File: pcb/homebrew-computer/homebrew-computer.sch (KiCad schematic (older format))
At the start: 0 parts

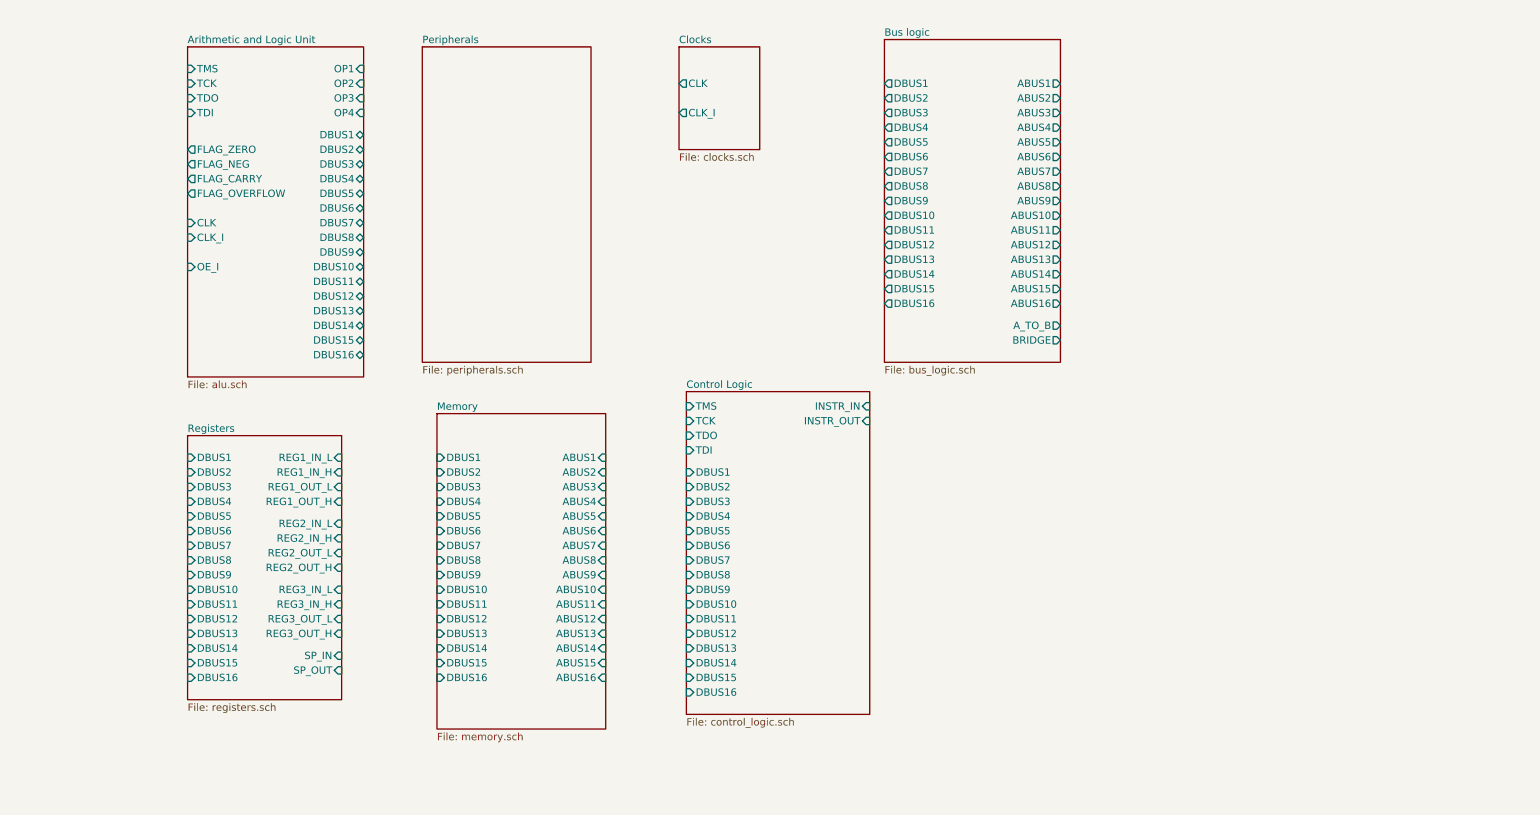
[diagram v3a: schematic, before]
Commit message: Add the memory interface logic
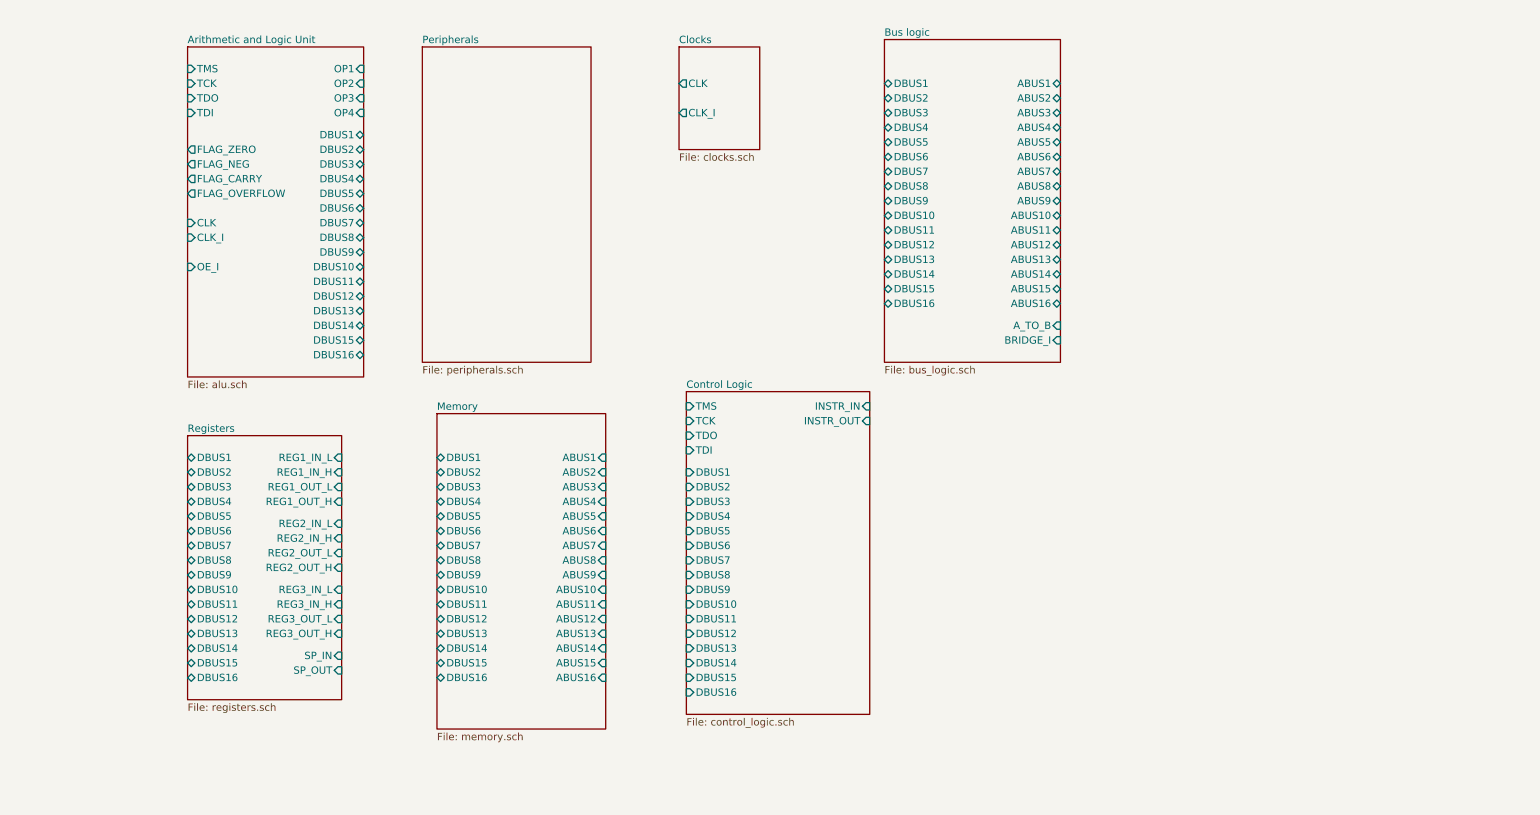
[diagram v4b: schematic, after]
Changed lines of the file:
@@
 F0 "Registers" 50
 F1 "registers.sch" 50
-F2 "DBUS1" I L 2250 3800 50
-F3 "DBUS2" I L 2250 3900 50
-F4 "DBUS3" I L 2250 4000 50
-F5 "DBUS4" I L 2250 4100 50
-F6 "DBUS5" I L 2250 4200 50
-F7 "DBUS6" I L 2250 4300 50
-F8 "DBUS7" I L 2250 4400 50
-F9 "DBUS8" I L 2250 4500 50
-F10 "DBUS9" I L 2250 4600 50
-F11 "DBUS10" I L 2250 4700 50
-F12 "DBUS11" I L 2250 4800 50
-F13 "DBUS12" I L 2250 4900 50
-F14 "DBUS13" I L 2250 5000 50
-F15 "DBUS14" I L 2250 5100 50
-F16 "DBUS15" I L 2250 5200 50
-F17 "DBUS16" I L 2250 5300 50
+F2 "DBUS1" B L 2250 3800 50
+F3 "DBUS2" B L 2250 3900 50
+F4 "DBUS3" B L 2250 4000 50
+F5 "DBUS4" B L 2250 4100 50
+F6 "DBUS5" B L 2250 4200 50
+F7 "DBUS6" B L 2250 4300 50
+F8 "DBUS7" B L 2250 4400 50
+F9 "DBUS8" B L 2250 4500 50
+F10 "DBUS9" B L 2250 4600 50
+F11 "DBUS10" B L 2250 4700 50
+F12 "DBUS11" B L 2250 4800 50
+F13 "DBUS12" B L 2250 4900 50
+F14 "DBUS13" B L 2250 5000 50
+F15 "DBUS14" B L 2250 5100 50
+F16 "DBUS15" B L 2250 5200 50
+F17 "DBUS16" B L 2250 5300 50
 F18 "REG1_IN_L" I R 3300 3800 50
 F19 "REG1_IN_H" I R 3300 3900 50
@@
 $EndSheet
 $Sheet
+S 5600 1000 550  700
+U 5F97DC64
+F0 "Clocks" 50
+F1 "clocks.sch" 50
+F2 "CLK" O L 5600 1250 50
+F3 "CLK_I" O L 5600 1450 50
+$EndSheet
+$Sheet
+S 7000 950  1200 2200
+U 5F97DCB2
+F0 "Bus logic" 50
+F1 "bus_logic.sch" 50
+F2 "DBUS1" B L 7000 1250 50
+F3 "DBUS2" B L 7000 1350 50
+F4 "DBUS3" B L 7000 1450 50
+F5 "DBUS4" B L 7000 1550 50
+F6 "DBUS5" B L 7000 1650 50
+F7 "DBUS6" B L 7000 1750 50
+F8 "DBUS7" B L 7000 1850 50
+F9 "DBUS8" B L 7000 1950 50
+F10 "DBUS9" B L 7000 2050 50
+F11 "DBUS10" B L 7000 2150 50
+F12 "DBUS11" B L 7000 2250 50
+F13 "DBUS12" B L 7000 2350 50
+F14 "DBUS13" B L 7000 2450 50
+F15 "DBUS14" B L 7000 2550 50
+F16 "DBUS15" B L 7000 2650 50
+F17 "DBUS16" B L 7000 2750 50
+F18 "ABUS1" B R 8200 1250 50
+F19 "ABUS2" B R 8200 1350 50
+F20 "ABUS3" B R 8200 1450 50
+F21 "ABUS4" B R 8200 1550 50
+F22 "ABUS5" B R 8200 1650 50
+F23 "ABUS6" B R 8200 1750 50
+F24 "ABUS7" B R 8200 1850 50
+F25 "ABUS8" B R 8200 1950 50
+F26 "ABUS9" B R 8200 2050 50
+F27 "ABUS10" B R 8200 2150 50
+F28 "ABUS11" B R 8200 2250 50
+F29 "ABUS12" B R 8200 2350 50
+F30 "ABUS13" B R 8200 2450 50
+F31 "ABUS14" B R 8200 2550 50
+F32 "ABUS15" B R 8200 2650 50
+F33 "ABUS16" B R 8200 2750 50
+F34 "A_TO_B" I R 8200 2900 50
+F35 "BRIDGE_I" I R 8200 3000 50
+$EndSheet
+$Sheet
 S 3950 3500 1150 2150
 U 5F95DC76
 F0 "Memory" 50
 F1 "memory.sch" 50
-F2 "DBUS1" I L 3950 3800 50
-F3 "DBUS2" I L 3950 3900 50
-F4 "DBUS3" I L 3950 4000 50
-F5 "DBUS4" I L 3950 4100 50
-F6 "DBUS5" I L 3950 4200 50
-F7 "DBUS6" I L 3950 4300 50
-F8 "DBUS7" I L 3950 4400 50
-F9 "DBUS8" I L 3950 4500 50
-F10 "DBUS9" I L 3950 4600 50
-F11 "DBUS10" I L 3950 4700 50
-F12 "DBUS11" I L 3950 4800 50
-F13 "DBUS12" I L 3950 4900 50
-F14 "DBUS13" I L 3950 5000 50
-F15 "DBUS14" I L 3950 5100 50
-F16 "DBUS15" I L 3950 5200 50
-F17 "DBUS16" I L 3950 5300 50
+F2 "DBUS1" B L 3950 3800 50
+F3 "DBUS2" B L 3950 3900 50
+F4 "DBUS3" B L 3950 4000 50
+F5 "DBUS4" B L 3950 4100 50
+F6 "DBUS5" B L 3950 4200 50
+F7 "DBUS6" B L 3950 4300 50
+F8 "DBUS7" B L 3950 4400 50
+F9 "DBUS8" B L 3950 4500 50
+F10 "DBUS9" B L 3950 4600 50
+F11 "DBUS10" B L 3950 4700 50
+F12 "DBUS11" B L 3950 4800 50
+F13 "DBUS12" B L 3950 4900 50
+F14 "DBUS13" B L 3950 5000 50
+F15 "DBUS14" B L 3950 5100 50
+F16 "DBUS15" B L 3950 5200 50
+F17 "DBUS16" B L 3950 5300 50
 F18 "ABUS1" I R 5100 3800 50
 F19 "ABUS2" I R 5100 3900 50
@@
 F33 "ABUS16" I R 5100 5300 50
 $EndSheet
-$Sheet
-S 5600 1000 550  700
-U 5F97DC64
-F0 "Clocks" 50
-F1 "clocks.sch" 50
-F2 "CLK" O L 5600 1250 50
-F3 "CLK_I" O L 5600 1450 50
-$EndSheet
-$Sheet
-S 7000 950  1200 2200
-U 5F97DCB2
-F0 "Bus logic" 50
-F1 "bus_logic.sch" 50
-F2 "DBUS1" O L 7000 1250 50
-F3 "DBUS2" O L 7000 1350 50
-F4 "DBUS3" O L 7000 1450 50
-F5 "DBUS4" O L 7000 1550 50
-F6 "DBUS5" O L 7000 1650 50
-F7 "DBUS6" O L 7000 1750 50
-F8 "DBUS7" O L 7000 1850 50
-F9 "DBUS8" O L 7000 1950 50
-F10 "DBUS9" O L 7000 2050 50
-F11 "DBUS10" O L 7000 2150 50
-F12 "DBUS11" O L 7000 2250 50
-F13 "DBUS12" O L 7000 2350 50
-F14 "DBUS13" O L 7000 2450 50
-F15 "DBUS14" O L 7000 2550 50
-F16 "DBUS15" O L 7000 2650 50
-F17 "DBUS16" O L 7000 2750 50
-F18 "ABUS1" O R 8200 1250 50
-F19 "ABUS2" O R 8200 1350 50
-F20 "ABUS3" O R 8200 1450 50
-F21 "ABUS4" O R 8200 1550 50
-F22 "ABUS5" O R 8200 1650 50
-F23 "ABUS6" O R 8200 1750 50
-F24 "ABUS7" O R 8200 1850 50
-F25 "ABUS8" O R 8200 1950 50
-F26 "ABUS9" O R 8200 2050 50
-F27 "ABUS10" O R 8200 2150 50
-F28 "ABUS11" O R 8200 2250 50
-F29 "ABUS12" O R 8200 2350 50
-F30 "ABUS13" O R 8200 2450 50
-F31 "ABUS14" O R 8200 2550 50
-F32 "ABUS15" O R 8200 2650 50
-F33 "ABUS16" O R 8200 2750 50
-F34 "A_TO_B" O R 8200 2900 50
-F35 "BRIDGE" O R 8200 3000 50
-$EndSheet
 $EndSCHEMATC

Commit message: Add beginning of peripheral ios
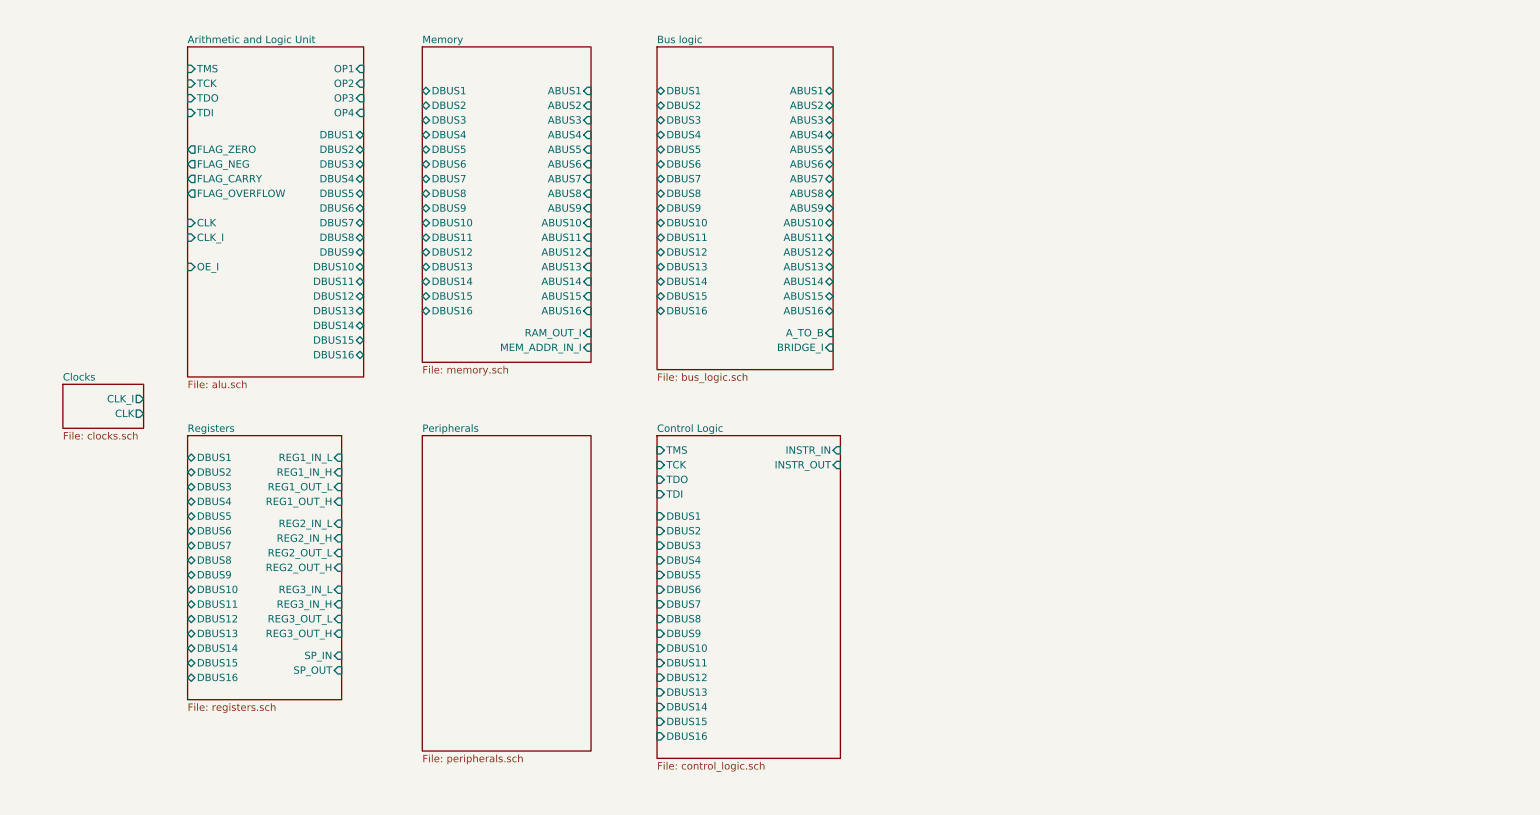
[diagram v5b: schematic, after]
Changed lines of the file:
@@
 $EndDescr
 $Sheet
-S 3850 1000 1150 2150
-U 5F8B5DB4
-F0 "Peripherals" 50
-F1 "peripherals.sch" 50
-$EndSheet
-$Sheet
-S 5650 3350 1250 2200
+S 5450 3650 1250 2200
 U 5F8B5E3D
 F0 "Control Logic" 50
 F1 "control_logic.sch" 50
-F2 "TMS" I L 5650 3450 50
-F3 "TCK" I L 5650 3550 50
-F4 "TDO" I L 5650 3650 50
-F5 "TDI" I L 5650 3750 50
-F6 "DBUS1" I L 5650 3900 50
-F7 "DBUS2" I L 5650 4000 50
-F8 "DBUS3" I L 5650 4100 50
-F9 "DBUS4" I L 5650 4200 50
-F10 "DBUS5" I L 5650 4300 50
-F11 "DBUS6" I L 5650 4400 50
-F12 "DBUS7" I L 5650 4500 50
-F13 "DBUS8" I L 5650 4600 50
-F14 "DBUS9" I L 5650 4700 50
-F15 "DBUS10" I L 5650 4800 50
-F16 "DBUS11" I L 5650 4900 50
-F17 "DBUS12" I L 5650 5000 50
-F18 "DBUS13" I L 5650 5100 50
-F19 "DBUS14" I L 5650 5200 50
-F20 "DBUS15" I L 5650 5300 50
-F21 "DBUS16" I L 5650 5400 50
-F22 "INSTR_IN" I R 6900 3450 50
-F23 "INSTR_OUT" I R 6900 3550 50
+F2 "TMS" I L 5450 3750 50
+F3 "TCK" I L 5450 3850 50
+F4 "TDO" I L 5450 3950 50
+F5 "TDI" I L 5450 4050 50
+F6 "DBUS1" I L 5450 4200 50
+F7 "DBUS2" I L 5450 4300 50
+F8 "DBUS3" I L 5450 4400 50
+F9 "DBUS4" I L 5450 4500 50
+F10 "DBUS5" I L 5450 4600 50
+F11 "DBUS6" I L 5450 4700 50
+F12 "DBUS7" I L 5450 4800 50
+F13 "DBUS8" I L 5450 4900 50
+F14 "DBUS9" I L 5450 5000 50
+F15 "DBUS10" I L 5450 5100 50
+F16 "DBUS11" I L 5450 5200 50
+F17 "DBUS12" I L 5450 5300 50
+F18 "DBUS13" I L 5450 5400 50
+F19 "DBUS14" I L 5450 5500 50
+F20 "DBUS15" I L 5450 5600 50
+F21 "DBUS16" I L 5450 5700 50
+F22 "INSTR_IN" I R 6700 3750 50
+F23 "INSTR_OUT" I R 6700 3850 50
 $EndSheet
 $Sheet
@@
 $EndSheet
 $Sheet
-S 5600 1000 550  700
+S 1400 3300 550  300
 U 5F97DC64
 F0 "Clocks" 50
 F1 "clocks.sch" 50
-F2 "CLK" O L 5600 1250 50
-F3 "CLK_I" O L 5600 1450 50
+F2 "CLK" O R 1950 3500 50
+F3 "CLK_I" O R 1950 3400 50
 $EndSheet
 $Sheet
-S 7000 950  1200 2200
+S 5450 1000 1200 2200
 U 5F97DCB2
 F0 "Bus logic" 50
 F1 "bus_logic.sch" 50
-F2 "DBUS1" B L 7000 1250 50
-F3 "DBUS2" B L 7000 1350 50
-F4 "DBUS3" B L 7000 1450 50
-F5 "DBUS4" B L 7000 1550 50
-F6 "DBUS5" B L 7000 1650 50
-F7 "DBUS6" B L 7000 1750 50
-F8 "DBUS7" B L 7000 1850 50
-F9 "DBUS8" B L 7000 1950 50
-F10 "DBUS9" B L 7000 2050 50
-F11 "DBUS10" B L 7000 2150 50
-F12 "DBUS11" B L 7000 2250 50
-F13 "DBUS12" B L 7000 2350 50
-F14 "DBUS13" B L 7000 2450 50
-F15 "DBUS14" B L 7000 2550 50
-F16 "DBUS15" B L 7000 2650 50
-F17 "DBUS16" B L 7000 2750 50
-F18 "ABUS1" B R 8200 1250 50
-F19 "ABUS2" B R 8200 1350 50
-F20 "ABUS3" B R 8200 1450 50
-F21 "ABUS4" B R 8200 1550 50
-F22 "ABUS5" B R 8200 1650 50
-F23 "ABUS6" B R 8200 1750 50
-F24 "ABUS7" B R 8200 1850 50
-F25 "ABUS8" B R 8200 1950 50
-F26 "ABUS9" B R 8200 2050 50
-F27 "ABUS10" B R 8200 2150 50
-F28 "ABUS11" B R 8200 2250 50
-F29 "ABUS12" B R 8200 2350 50
-F30 "ABUS13" B R 8200 2450 50
-F31 "ABUS14" B R 8200 2550 50
-F32 "ABUS15" B R 8200 2650 50
-F33 "ABUS16" B R 8200 2750 50
-F34 "A_TO_B" I R 8200 2900 50
-F35 "BRIDGE_I" I R 8200 3000 50
+F2 "DBUS1" B L 5450 1300 50
+F3 "DBUS2" B L 5450 1400 50
+F4 "DBUS3" B L 5450 1500 50
+F5 "DBUS4" B L 5450 1600 50
+F6 "DBUS5" B L 5450 1700 50
+F7 "DBUS6" B L 5450 1800 50
+F8 "DBUS7" B L 5450 1900 50
+F9 "DBUS8" B L 5450 2000 50
+F10 "DBUS9" B L 5450 2100 50
+F11 "DBUS10" B L 5450 2200 50
+F12 "DBUS11" B L 5450 2300 50
+F13 "DBUS12" B L 5450 2400 50
+F14 "DBUS13" B L 5450 2500 50
+F15 "DBUS14" B L 5450 2600 50
+F16 "DBUS15" B L 5450 2700 50
+F17 "DBUS16" B L 5450 2800 50
+F18 "ABUS1" B R 6650 1300 50
+F19 "ABUS2" B R 6650 1400 50
+F20 "ABUS3" B R 6650 1500 50
+F21 "ABUS4" B R 6650 1600 50
+F22 "ABUS5" B R 6650 1700 50
+F23 "ABUS6" B R 6650 1800 50
+F24 "ABUS7" B R 6650 1900 50
+F25 "ABUS8" B R 6650 2000 50
+F26 "ABUS9" B R 6650 2100 50
+F27 "ABUS10" B R 6650 2200 50
+F28 "ABUS11" B R 6650 2300 50
+F29 "ABUS12" B R 6650 2400 50
+F30 "ABUS13" B R 6650 2500 50
+F31 "ABUS14" B R 6650 2600 50
+F32 "ABUS15" B R 6650 2700 50
+F33 "ABUS16" B R 6650 2800 50
+F34 "A_TO_B" I R 6650 2950 50
+F35 "BRIDGE_I" I R 6650 3050 50
 $EndSheet
 $Sheet
-S 3950 3500 1150 2150
+S 3850 1000 1150 2150
 U 5F95DC76
 F0 "Memory" 50
 F1 "memory.sch" 50
-F2 "DBUS1" B L 3950 3800 50
-F3 "DBUS2" B L 3950 3900 50
-F4 "DBUS3" B L 3950 4000 50
-F5 "DBUS4" B L 3950 4100 50
-F6 "DBUS5" B L 3950 4200 50
-F7 "DBUS6" B L 3950 4300 50
-F8 "DBUS7" B L 3950 4400 50
-F9 "DBUS8" B L 3950 4500 50
-F10 "DBUS9" B L 3950 4600 50
-F11 "DBUS10" B L 3950 4700 50
-F12 "DBUS11" B L 3950 4800 50
-F13 "DBUS12" B L 3950 4900 50
-F14 "DBUS13" B L 3950 5000 50
-F15 "DBUS14" B L 3950 5100 50
-F16 "DBUS15" B L 3950 5200 50
-F17 "DBUS16" B L 3950 5300 50
-F18 "ABUS1" I R 5100 3800 50
-F19 "ABUS2" I R 5100 3900 50
-F20 "ABUS3" I R 5100 4000 50
-F21 "ABUS4" I R 5100 4100 50
-F22 "ABUS5" I R 5100 4200 50
-F23 "ABUS6" I R 5100 4300 50
-F24 "ABUS7" I R 5100 4400 50
-F25 "ABUS8" I R 5100 4500 50
-F26 "ABUS9" I R 5100 4600 50
-F27 "ABUS10" I R 5100 4700 50
-F28 "ABUS11" I R 5100 4800 50
-F29 "ABUS12" I R 5100 4900 50
-F30 "ABUS13" I R 5100 5000 50
-F31 "ABUS14" I R 5100 5100 50
-F32 "ABUS15" I R 5100 5200 50
-F33 "ABUS16" I R 5100 5300 50
+F2 "DBUS1" B L 3850 1300 50
+F3 "DBUS2" B L 3850 1400 50
+F4 "DBUS3" B L 3850 1500 50
+F5 "DBUS4" B L 3850 1600 50
+F6 "DBUS5" B L 3850 1700 50
+F7 "DBUS6" B L 3850 1800 50
+F8 "DBUS7" B L 3850 1900 50
+F9 "DBUS8" B L 3850 2000 50
+F10 "DBUS9" B L 3850 2100 50
+F11 "DBUS10" B L 3850 2200 50
+F12 "DBUS11" B L 3850 2300 50
+F13 "DBUS12" B L 3850 2400 50
+F14 "DBUS13" B L 3850 2500 50
+F15 "DBUS14" B L 3850 2600 50
+F16 "DBUS15" B L 3850 2700 50
+F17 "DBUS16" B L 3850 2800 50
+F18 "ABUS1" I R 5000 1300 50
+F19 "ABUS2" I R 5000 1400 50
+F20 "ABUS3" I R 5000 1500 50
+F21 "ABUS4" I R 5000 1600 50
+F22 "ABUS5" I R 5000 1700 50
+F23 "ABUS6" I R 5000 1800 50
+F24 "ABUS7" I R 5000 1900 50
+F25 "ABUS8" I R 5000 2000 50
+F26 "ABUS9" I R 5000 2100 50
+F27 "ABUS10" I R 5000 2200 50
+F28 "ABUS11" I R 5000 2300 50
+F29 "ABUS12" I R 5000 2400 50
+F30 "ABUS13" I R 5000 2500 50
+F31 "ABUS14" I R 5000 2600 50
+F32 "ABUS15" I R 5000 2700 50
+F33 "ABUS16" I R 5000 2800 50
+F34 "RAM_OUT_I" I R 5000 2950 50
+F35 "MEM_ADDR_IN_I" I R 5000 3050 50
+$EndSheet
+$Sheet
+S 3850 3650 1150 2150
+U 5F8B5DB4
+F0 "Peripherals" 50
+F1 "peripherals.sch" 50
 $EndSheet
 $EndSCHEMATC
